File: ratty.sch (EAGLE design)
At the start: 89 parts, among them IC2 L293DD, Q1 BS170, Q2 BS170, Q3 BS170, Q5 BS170, U1 ITG-32001:1

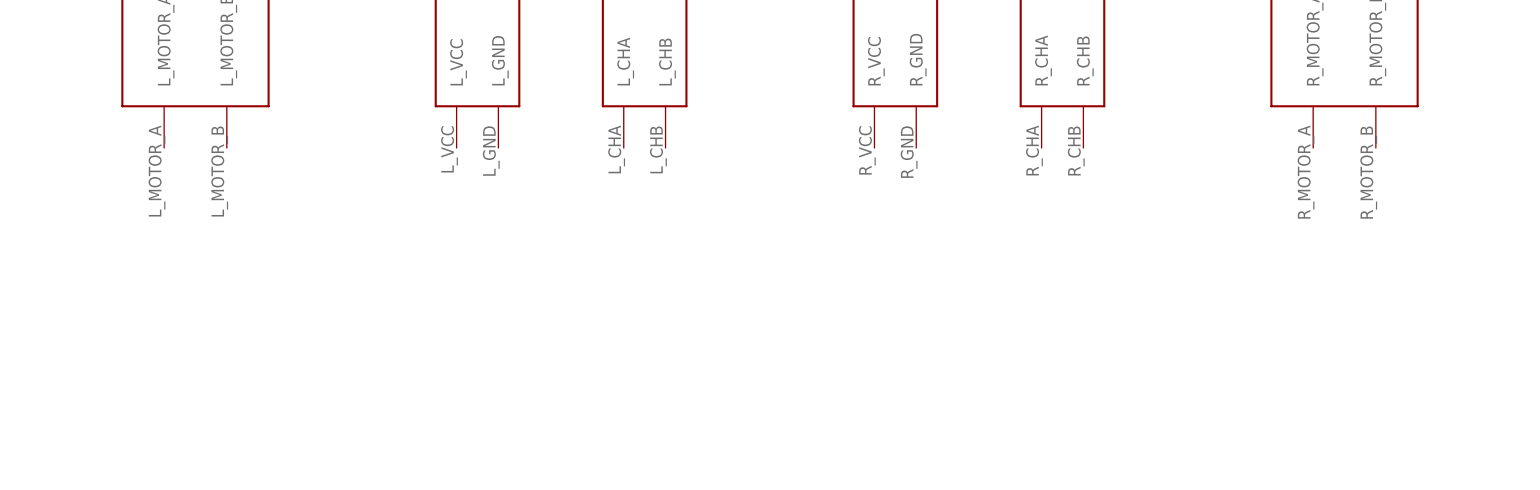
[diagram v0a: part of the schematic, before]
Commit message: Finished motor schematic and placed led/sensors on board
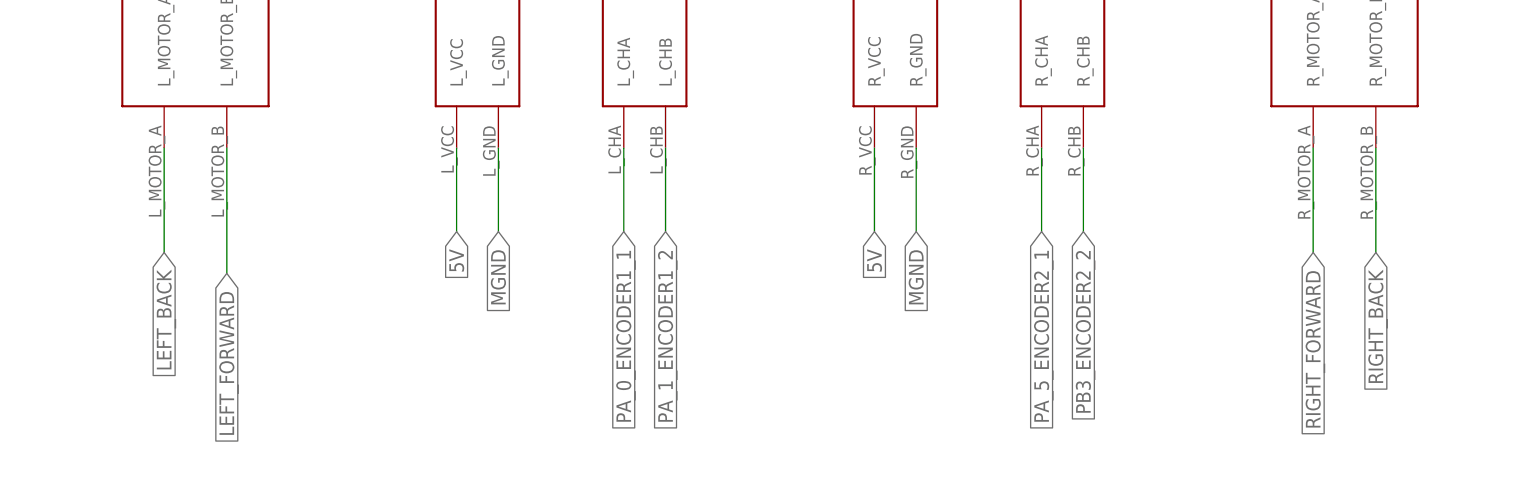
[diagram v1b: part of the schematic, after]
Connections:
- new net PA_0_ENCODER1_1: U$8.L_CHA
- new net PA_1_ENCODER1_2: U$8.L_CHB
- net 5V: now also U$8.L_VCC, U$8.R_VCC
- net LEFT_BACK: now also U$8.L_MOTOR_A
- net LEFT_FORWARD: now also U$8.L_MOTOR_B
- net MGND: now also U$8.L_GND, U$8.R_GND
- net PA_5_ENCODER2_1: now also U$8.R_CHA
- net PB3_ENCODER2_2: now also U$8.R_CHB
- net RIGHT_BACK: now also U$8.R_MOTOR_B
- net RIGHT_FORWARD: now also U$8.R_MOTOR_A
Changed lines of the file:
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@@
 <?xml version="1.0" encoding="utf-8"?>
 <!DOCTYPE eagle SYSTEM "eagle.dtd">
-<eagle version="7.5.0">
+<eagle version="7.7.0">
 <drawing>
 <settings>
@@
 <wire x1="350.52" y1="172.72" x2="350.52" y2="175.26" width="0.1524" layer="91"/>
 </segment>
+<segment>
+<pinref part="U$8" gate="G$1" pin="L_VCC"/>
+<wire x1="325.12" y1="-5.08" x2="325.12" y2="-15.24" width="0.1524" layer="91"/>
+<label x="325.12" y="-15.24" size="1.778" layer="95" rot="R270" xref="yes"/>
+</segment>
+<segment>
+<pinref part="U$8" gate="G$1" pin="R_VCC"/>
+<wire x1="375.92" y1="-5.08" x2="375.92" y2="-15.24" width="0.1524" layer="91"/>
+<label x="375.92" y="-15.24" size="1.778" layer="95" rot="R270" xref="yes"/>
+</segment>
 </net>
 <net name="N$4" class="0">
@@
 <label x="256.54" y="45.72" size="1.778" layer="95" xref="yes"/>
 </segment>
+<segment>
+<pinref part="U$8" gate="G$1" pin="L_MOTOR_B"/>
+<wire x1="297.18" y1="-5.08" x2="297.18" y2="-20.32" width="0.1524" layer="91"/>
+<label x="297.18" y="-20.32" size="1.778" layer="95" rot="R270" xref="yes"/>
+</segment>
 </net>
 <net name="LEFT_BACK" class="0">
@@
 <label x="256.54" y="40.64" size="1.778" layer="95" xref="yes"/>
 </segment>
+<segment>
+<pinref part="U$8" gate="G$1" pin="L_MOTOR_A"/>
+<wire x1="289.56" y1="-5.08" x2="289.56" y2="-17.78" width="0.1524" layer="91"/>
+<label x="289.56" y="-17.78" size="1.778" layer="95" rot="R270" xref="yes"/>
+</segment>
 </net>
 <net name="RIGHT_BACK" class="0">
@@
 <label x="256.54" y="35.56" size="1.778" layer="95" xref="yes"/>
 </segment>
+<segment>
+<pinref part="U$8" gate="G$1" pin="R_MOTOR_B"/>
+<wire x1="436.88" y1="-5.08" x2="436.88" y2="-17.78" width="0.1524" layer="91"/>
+<label x="436.88" y="-17.78" size="1.778" layer="95" rot="R270" xref="yes"/>
+</segment>
 </net>
 <net name="RIGHT_FORWARD" class="0">
@@
 <wire x1="246.38" y1="30.48" x2="256.54" y2="30.48" width="0.1524" layer="91"/>
 <label x="256.54" y="30.48" size="1.778" layer="95" xref="yes"/>
+</segment>
+<segment>
+<pinref part="U$8" gate="G$1" pin="R_MOTOR_A"/>
+<wire x1="429.26" y1="-5.08" x2="429.26" y2="-17.78" width="0.1524" layer="91"/>
+<label x="429.26" y="-17.78" size="1.778" layer="95" rot="R270" xref="yes"/>
 </segment>
 </net>
@@
 <label x="213.36" y="330.2" size="1.778" layer="95" xref="yes"/>
 </segment>
+<segment>
+<pinref part="U$8" gate="G$1" pin="L_CHA"/>
+<wire x1="345.44" y1="-5.08" x2="345.44" y2="-15.24" width="0.1524" layer="91"/>
+<label x="345.44" y="-15.24" size="1.778" layer="95" rot="R270" xref="yes"/>
+</segment>
 </net>
 <net name="PA_1_ENCODER1_2" class="0">
@@
 <wire x1="203.2" y1="327.66" x2="213.36" y2="327.66" width="0.1524" layer="91"/>
 <label x="213.36" y="327.66" size="1.778" layer="95" xref="yes"/>
+</segment>
+<segment>
+<pinref part="U$8" gate="G$1" pin="L_CHB"/>
+<wire x1="350.52" y1="-5.08" x2="350.52" y2="-15.24" width="0.1524" layer="91"/>
+<label x="350.52" y="-15.24" size="1.778" layer="95" rot="R270" xref="yes"/>
 </segment>
 </net>
@@
 <label x="246.38" y="7.62" size="1.778" layer="95" rot="R270" xref="yes"/>
 </segment>
+<segment>
+<pinref part="U$8" gate="G$1" pin="L_GND"/>
+<wire x1="330.2" y1="-5.08" x2="330.2" y2="-15.24" width="0.1524" layer="91"/>
+<label x="330.2" y="-15.24" size="1.778" layer="95" rot="R270" xref="yes"/>
+</segment>
+<segment>
+<pinref part="U$8" gate="G$1" pin="R_GND"/>
+<wire x1="381" y1="-5.08" x2="381" y2="-15.24" width="0.1524" layer="91"/>
+<label x="381" y="-15.24" size="1.778" layer="95" rot="R270" xref="yes"/>
+</segment>
 </net>
 <net name="N$2" class="0">
@@
 <label x="213.36" y="276.86" size="1.778" layer="95" xref="yes"/>
 </segment>
+<segment>
+<pinref part="U$8" gate="G$1" pin="R_CHB"/>
+<wire x1="401.32" y1="-5.08" x2="401.32" y2="-15.24" width="0.1524" layer="91"/>
+<label x="401.32" y="-15.24" size="1.778" layer="95" rot="R270" xref="yes"/>
+</segment>
 </net>
 <net name="PA_7_REC_CIRCUIT_1" class="0">
@@
 <label x="208.28" y="317.5" size="1.778" layer="95" xref="yes"/>
 </segment>
-</net>
+<segment>
+<pinref part="U$8" gate="G$1" pin="R_CHA"/>
+<wire x1="396.24" y1="-5.08" x2="396.24" y2="-15.24" width="0.1524" layer="91"/>
+<label x="396.24" y="-15.24" size="1.778" layer="95" rot="R270" xref="yes"/>
+</segment>
+</net>

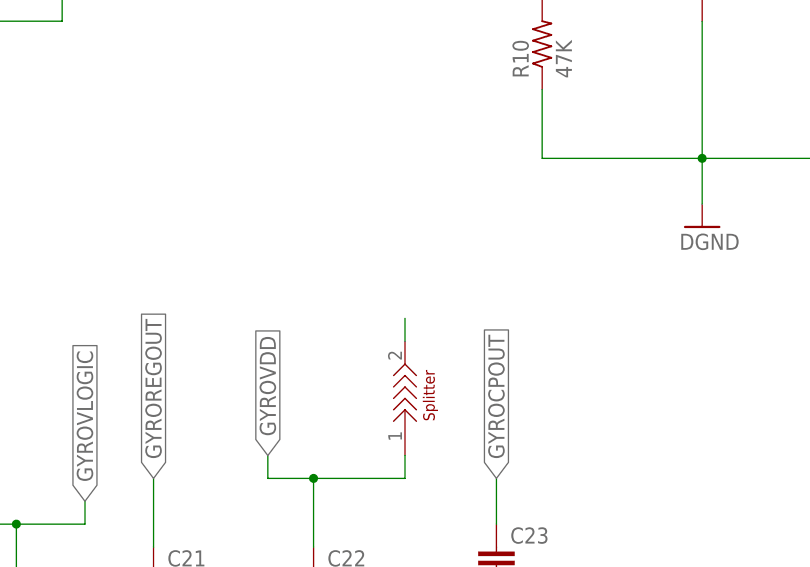
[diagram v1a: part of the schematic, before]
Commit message: Placed all parts. Drew top and bot layers
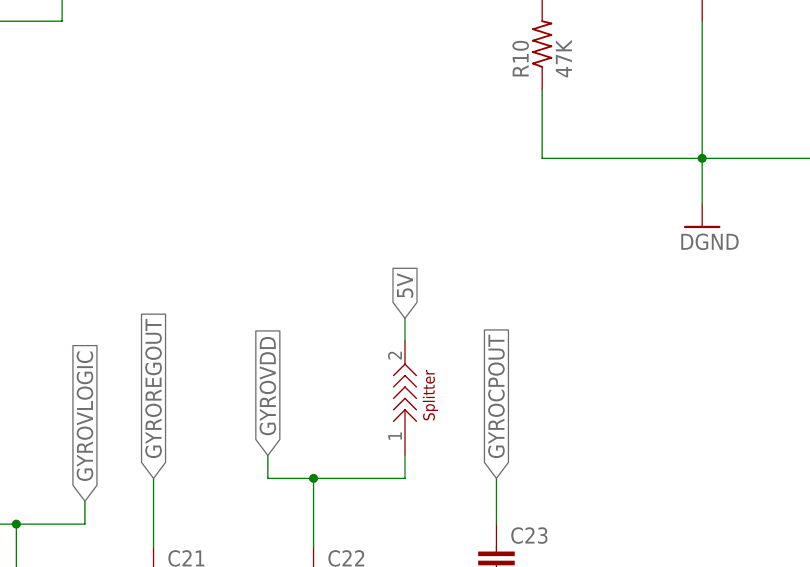
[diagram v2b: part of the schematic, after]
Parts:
- renumbered U$10 to SPLIT_GYRO_VDD, U$12 to SPLIT_GYRO_LOGIC, U$14 to SPLIT_VSS_CAP, U$20 to D_SPLITTER, U$21 to A_SPLITTER, U$7 to M_SPLITTER
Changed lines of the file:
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@@
 <part name="GND17" library="supply1" deviceset="GND" device=""/>
 <part name="GND16" library="supply1" deviceset="GND" device=""/>
-<part name="U$20" library="splitter" deviceset="SPLITTER" device=""/>
-<part name="U$21" library="splitter" deviceset="SPLITTER" device=""/>
+<part name="D_SPLITTER" library="splitter" deviceset="SPLITTER" device=""/>
+<part name="A_SPLITTER" library="splitter" deviceset="SPLITTER" device=""/>
 <part name="GND1" library="SparkFun-Aesthetics" deviceset="GND" device=""/>
 <part name="AGND1" library="supply1" deviceset="AGND" device=""/>
@@
 <part name="AGND5" library="supply1" deviceset="AGND" device=""/>
 <part name="AGND6" library="supply1" deviceset="AGND" device=""/>
-<part name="U$7" library="splitter" deviceset="SPLITTER" device=""/>
+<part name="M_SPLITTER" library="splitter" deviceset="SPLITTER" device=""/>
 <part name="GND4" library="SparkFun-Aesthetics" deviceset="DGND" device=""/>
 <part name="GND6" library="SparkFun-Aesthetics" deviceset="DGND" device=""/>
@@
 <part name="GND14" library="SparkFun-Aesthetics" deviceset="DGND" device=""/>
 <part name="R8" library="rcl" deviceset="R-US_" device="R0603" value="100"/>
-<part name="U$10" library="splitter" deviceset="SPLITTER" device=""/>
-<part name="U$12" library="splitter" deviceset="SPLITTER" device=""/>
+<part name="SPLIT_GYRO_VDD" library="splitter" deviceset="SPLITTER" device=""/>
+<part name="SPLIT_GYRO_LOGIC" library="splitter" deviceset="SPLITTER" device=""/>
 <part name="JP1" library="pinhead" deviceset="PINHD-1X5" device=""/>
 <part name="C26" library="rcl" deviceset="C-EU" device="C0603" value="4.7uF"/>
-<part name="U$14" library="splitter" deviceset="SPLITTER" device=""/>
+<part name="SPLIT_VSS_CAP" library="splitter" deviceset="SPLITTER" device=""/>
 <part name="U$17" library="LEDs" deviceset="LED-TRICOLOR" device=""/>
 <part name="GND15" library="SparkFun-Aesthetics" deviceset="DGND" device=""/>
@@
 <instance part="GND17" gate="1" x="254" y="147.32" rot="R90"/>
 <instance part="GND16" gate="1" x="261.62" y="149.86" rot="R90"/>
-<instance part="U$20" gate="G$1" x="43.18" y="53.34" rot="R180"/>
-<instance part="U$21" gate="G$1" x="43.18" y="60.96" rot="R180"/>
+<instance part="D_SPLITTER" gate="G$1" x="43.18" y="53.34" rot="R180"/>
+<instance part="A_SPLITTER" gate="G$1" x="43.18" y="60.96" rot="R180"/>
 <instance part="GND1" gate="1" x="50.8" y="43.18"/>
 <instance part="AGND1" gate="VR1" x="35.56" y="60.96" rot="R270"/>
@@
 <instance part="AGND5" gate="VR1" x="553.72" y="109.22"/>
 <instance part="AGND6" gate="VR1" x="599.44" y="109.22"/>
-<instance part="U$7" gate="G$1" x="43.18" y="71.12" rot="R180"/>
+<instance part="M_SPLITTER" gate="G$1" x="43.18" y="71.12" rot="R180"/>
 <instance part="GND4" gate="G$1" x="596.9" y="190.5"/>
 <instance part="GND6" gate="G$1" x="492.76" y="187.96"/>
@@
 <instance part="GND14" gate="G$1" x="360.68" y="134.62"/>
 <instance part="R8" gate="G$1" x="-12.7" y="294.64"/>
-<instance part="U$10" gate="G$1" x="350.52" y="167.64" rot="R90"/>
-<instance part="U$12" gate="G$1" x="294.64" y="160.02" rot="R90"/>
+<instance part="SPLIT_GYRO_VDD" gate="G$1" x="350.52" y="167.64" rot="R90"/>
+<instance part="SPLIT_GYRO_LOGIC" gate="G$1" x="294.64" y="160.02" rot="R90"/>
 <instance part="JP1" gate="A" x="259.08" y="299.72"/>
 <instance part="C26" gate="G$1" x="213.36" y="223.52" rot="R90"/>
-<instance part="U$14" gate="G$1" x="55.88" y="220.98" rot="R270"/>
+<instance part="SPLIT_VSS_CAP" gate="G$1" x="55.88" y="220.98" rot="R270"/>
 <instance part="U$17" gate="G$1" x="144.78" y="193.04"/>
 <instance part="GND15" gate="G$1" x="177.8" y="190.5" rot="R90"/>
@@
 <wire x1="50.8" y1="78.74" x2="58.42" y2="78.74" width="0.1524" layer="91"/>
 <pinref part="GND1" gate="1" pin="GND"/>
-<pinref part="U$21" gate="G$1" pin="1"/>
+<pinref part="A_SPLITTER" gate="G$1" pin="1"/>
 <junction x="50.8" y="60.96"/>
-<pinref part="U$20" gate="G$1" pin="1"/>
+<pinref part="D_SPLITTER" gate="G$1" pin="1"/>
 <junction x="50.8" y="53.34"/>
-<pinref part="U$7" gate="G$1" pin="1"/>
+<pinref part="M_SPLITTER" gate="G$1" pin="1"/>
 <junction x="50.8" y="71.12"/>
 </segment>
 <segment>
 <pinref part="GND18" gate="G$1" pin="GND"/>
-<pinref part="U$20" gate="G$1" pin="2"/>
+<pinref part="D_SPLITTER" gate="G$1" pin="2"/>
 </segment>
 </net>
@@
 </segment>
 <segment>
-<pinref part="U$10" gate="G$1" pin="2"/>
+<pinref part="SPLIT_GYRO_VDD" gate="G$1" pin="2"/>
 <wire x1="350.52" y1="172.72" x2="350.52" y2="175.26" width="0.1524" layer="91"/>
+<label x="350.52" y="175.26" size="1.778" layer="95" rot="R90" xref="yes"/>
 </segment>
 <segment>
@@
 <net name="AGND" class="0">
 <segment>
-<pinref part="U$21" gate="G$1" pin="2"/>
+<pinref part="A_SPLITTER" gate="G$1" pin="2"/>
 <pinref part="AGND1" gate="VR1" pin="AGND"/>
 </segment>
@@
 <wire x1="350.52" y1="157.48" x2="350.52" y2="160.02" width="0.1524" layer="91"/>
 <label x="335.28" y="160.02" size="1.778" layer="95" rot="R90" xref="yes"/>
-<pinref part="U$10" gate="G$1" pin="1"/>
+<pinref part="SPLIT_GYRO_VDD" gate="G$1" pin="1"/>
 </segment>
 </net>
@@
 <wire x1="314.96" y1="152.4" x2="314.96" y2="154.94" width="0.1524" layer="91"/>
 <label x="314.96" y="154.94" size="1.778" layer="95" rot="R90" xref="yes"/>
-<pinref part="U$12" gate="G$1" pin="1"/>
+<pinref part="SPLIT_GYRO_LOGIC" gate="G$1" pin="1"/>
 </segment>
 </net>
@@
 <pinref part="GND20" gate="G$1" pin="GND"/>
 <wire x1="60.96" y1="228.6" x2="55.88" y2="228.6" width="0.1524" layer="91"/>
-<pinref part="U$14" gate="G$1" pin="1"/>
+<pinref part="SPLIT_VSS_CAP" gate="G$1" pin="1"/>
 <wire x1="55.88" y1="228.6" x2="45.72" y2="228.6" width="0.1524" layer="91"/>
 <junction x="55.88" y="228.6"/>
@@
 <net name="MGND" class="0">
 <segment>
-<pinref part="U$7" gate="G$1" pin="2"/>
+<pinref part="M_SPLITTER" gate="G$1" pin="2"/>
 <wire x1="38.1" y1="71.12" x2="33.02" y2="71.12" width="0.1524" layer="91"/>
 <label x="33.02" y="71.12" size="1.778" layer="95" rot="R180" xref="yes"/>
@@
 </segment>
 <segment>
-<pinref part="U$12" gate="G$1" pin="2"/>
+<pinref part="SPLIT_GYRO_LOGIC" gate="G$1" pin="2"/>
 <wire x1="294.64" y1="165.1" x2="294.64" y2="167.64" width="0.1524" layer="91"/>
 <label x="294.64" y="167.64" size="1.778" layer="95" rot="R90" xref="yes"/>
@@
 </segment>
 <segment>
-<pinref part="U$14" gate="G$1" pin="2"/>
+<pinref part="SPLIT_VSS_CAP" gate="G$1" pin="2"/>
 <wire x1="55.88" y1="215.9" x2="55.88" y2="210.82" width="0.1524" layer="91"/>
 <label x="55.88" y="210.82" size="1.778" layer="95" rot="R270" xref="yes"/>
